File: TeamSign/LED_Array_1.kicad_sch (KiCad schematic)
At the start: 56 parts

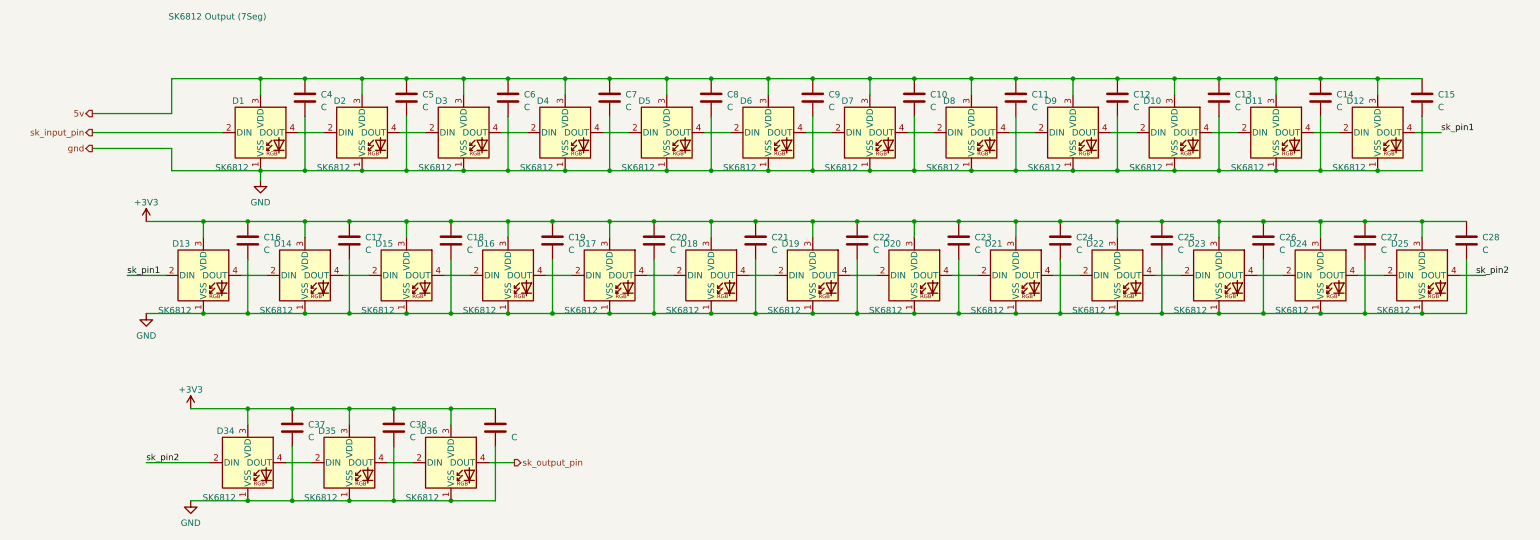
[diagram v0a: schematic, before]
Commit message: Add PEM nut footprint starter to library, also did small tweaks to BOM and updated symbols to include the barrel jack antics.  Yay!
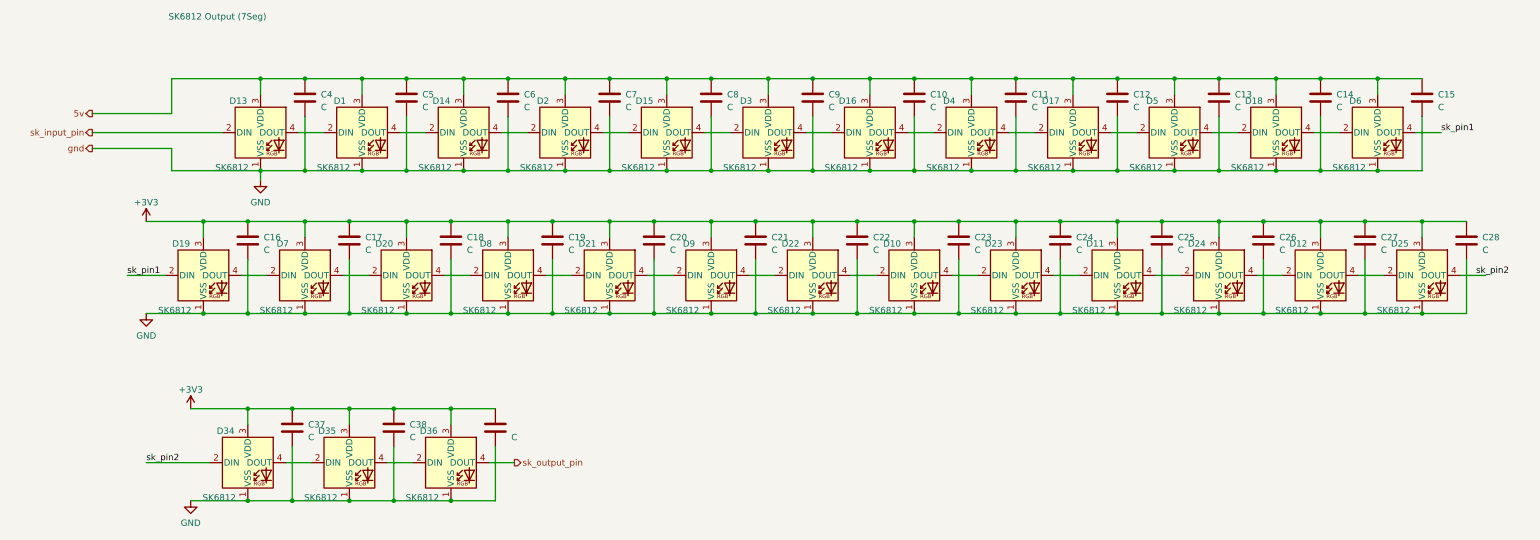
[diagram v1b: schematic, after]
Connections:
- net +3V3: now also D10.3 (VDD), D11.3 (VDD), D12.3 (VDD), D7.3 (VDD), D8.3 (VDD), D9.3 (VDD); no longer D13.3 (VDD), D14.3 (VDD), D15.3 (VDD), D16.3 (VDD), D17.3 (VDD), D18.3 (VDD)
- net 5v: now also D13.3 (VDD), D14.3 (VDD), D15.3 (VDD), D16.3 (VDD), D17.3 (VDD), D18.3 (VDD); no longer D10.3 (VDD), D11.3 (VDD), D12.3 (VDD), D7.3 (VDD), D8.3 (VDD), D9.3 (VDD)
- net sk_input_pin: now also D13.2 (DIN); no longer D1.2 (DIN)
- net sk_pin1: now also D19.2 (DIN), D6.4 (DOUT); no longer D12.4 (DOUT), D13.2 (DIN)
- net at D17.2 (DIN): now also D4.4 (DOUT); no longer D16.4 (DOUT)
- net at D17.4 (DOUT): now also D5.2 (DIN); no longer D18.2 (DIN)
- net at D2.2 (DIN): now also D14.4 (DOUT); no longer D1.4 (DOUT)
- net at D2.4 (DOUT): now also D15.2 (DIN); no longer D3.2 (DIN)
- net at D6.2 (DIN): now also D18.4 (DOUT); no longer D5.4 (DOUT)
- net at D7.2 (DIN): now also D19.4 (DOUT); no longer D6.4 (DOUT)
- net at D8.2 (DIN): now also D20.4 (DOUT); no longer D7.4 (DOUT)
- net at D8.4 (DOUT): now also D21.2 (DIN); no longer D9.2 (DIN)
- net at D9.4 (DOUT): now also D22.2 (DIN); no longer D10.2 (DIN)
- net at D15.4 (DOUT): now also D3.2 (DIN); no longer D16.2 (DIN)
- net at D20.2 (DIN): now also D7.4 (DOUT); no longer D19.4 (DOUT)
- net at D21.4 (DOUT): now also D9.2 (DIN); no longer D22.2 (DIN)
- net at D22.4 (DOUT): now also D10.2 (DIN); no longer D23.2 (DIN)
- net at D23.4 (DOUT): now also D11.2 (DIN); no longer D24.2 (DIN)
- net at D4.2 (DIN): now also D16.4 (DOUT); no longer D3.4 (DOUT)
- net at D10.4 (DOUT): now also D23.2 (DIN); no longer D11.2 (DIN)
- net at D11.4 (DOUT): now also D24.2 (DIN); no longer D12.2 (DIN)
- net at D24.4 (DOUT): now also D12.2 (DIN); no longer D25.2 (DIN)
- net at D13.4 (DOUT): now also D1.2 (DIN); no longer D14.2 (DIN)
- new net: D18.2 (DIN), D5.4 (DOUT)
- new net: D16.2 (DIN), D3.4 (DOUT)
- new net: D12.4 (DOUT), D25.2 (DIN)
- new net: D1.4 (DOUT), D14.2 (DIN)
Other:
- moved on the sheet: D1, D10, D11, D12, D13, D14, D15, D16, D17, D18, D19, D2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

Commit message: Place caps :)
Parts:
- removed C10, C11, C12, C13, C14, C15, C16, C17, C18, C19, C20, C21, C22, C23, C24, C25, C26, C27, C28, C37, C38, C39, C5, C6, C7, C8, C9: C, symbol Device:C
- added C4 (x27): 100nF, Capacitor_SMD:C_1206_3216Metric_Pad1.33x1.80mm_HandSolder, symbol Device:C
- C4: value C -> 100nF; footprint (none) -> Capacitor_SMD:C_1206_3216Metric_Pad1.33x1.80mm_HandSolder
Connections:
- net +3V3: now also C4.1, C4.1, C4.1, C4.1, C4.1, C4.1, C4.1, C4.1, C4.1, C4.1, C4.1, C4.1, C4.1, C4.1, C4.1, C4.1
- net 5v: now also C4.1, C4.1, C4.1, C4.1, C4.1, C4.1, C4.1, C4.1, C4.1, C4.1, C4.1
- net GND: now also C4.2, C4.2, C4.2, C4.2, C4.2, C4.2, C4.2, C4.2, C4.2, C4.2, C4.2, C4.2, C4.2, C4.2, C4.2, C4.2, C4.2, C4.2, C4.2, C4.2, C4.2, C4.2, C4.2, C4.2, C4.2, C4.2, C4.2

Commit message: Resolve subsheet antics... Yay.
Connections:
- net +3V3 is gone; now on net 5v: C4.1, C4.1, C4.1, C4.1, C4.1, C4.1, C4.1, C4.1, C4.1, C4.1, C4.1, C4.1, C4.1, C4.1, C4.1, C4.1, D10.3 (VDD), D11.3 (VDD), D12.3 (VDD), D19.3 (VDD), D20.3 (VDD), D21.3 (VDD), D22.3 (VDD), D23.3 (VDD), D24.3 (VDD), D25.3 (VDD), D34.3 (VDD), D35.3 (VDD), D36.3 (VDD), D7.3 (VDD), D8.3 (VDD), D9.3 (VDD)
- net sk_input_pin: now also D19.2 (DIN); no longer D13.2 (DIN)
- net sk_output_pin: now also D25.4 (DOUT); no longer D36.4 (DOUT)
- net sk_pin1: now also D15.2 (DIN), D21.4 (DOUT); no longer D19.2 (DIN), D6.4 (DOUT)
- net sk_pin2: now also D12.2 (DIN), D18.4 (DOUT); no longer D25.4 (DOUT), D34.2 (DIN)
- net at D17.2 (DIN): now also D23.4 (DOUT); no longer D4.4 (DOUT)
- net at D17.4 (DOUT): now also D11.2 (DIN); no longer D5.2 (DIN)
- net at D34.4 (DOUT): now also D13.2 (DIN); no longer D35.2 (DIN)
- net at D2.2 (DIN): now also D8.4 (DOUT); no longer D14.4 (DOUT)
- net at D2.4 (DOUT): now also D21.2 (DIN); no longer D15.2 (DIN)
- net at D6.2 (DIN): now also D12.4 (DOUT); no longer D18.4 (DOUT)
- net at D8.2 (DIN): now also D14.4 (DOUT); no longer D20.4 (DOUT)
- net at D9.2 (DIN): now also D15.4 (DOUT); no longer D21.4 (DOUT)
- net at D9.4 (DOUT): now also D3.2 (DIN); no longer D22.2 (DIN)
- net at D19.4 (DOUT): now also D34.2 (DIN); no longer D7.2 (DIN)
- net at D7.4 (DOUT): now also D35.2 (DIN); no longer D20.2 (DIN)
- net at D18.2 (DIN): now also D24.4 (DOUT); no longer D5.4 (DOUT)
- net at D22.4 (DOUT): now also D16.2 (DIN); no longer D10.2 (DIN)
- net at D23.2 (DIN): now also D4.4 (DOUT); no longer D10.4 (DOUT)
- net at D4.2 (DIN): now also D10.4 (DOUT); no longer D16.4 (DOUT)
- net at D36.2 (DIN): now also D20.4 (DOUT); no longer D35.4 (DOUT)
- net at D11.4 (DOUT): now also D5.2 (DIN); no longer D24.2 (DIN)
- net at D3.4 (DOUT): now also D22.2 (DIN); no longer D16.2 (DIN)
- net at D25.2 (DIN): now also D6.4 (DOUT); no longer D12.4 (DOUT)
- net at D13.4 (DOUT): now also D7.2 (DIN); no longer D1.2 (DIN)
- net at D1.4 (DOUT): now also D20.2 (DIN); no longer D14.2 (DIN)
- new net: D24.2 (DIN), D5.4 (DOUT)
- new net: D1.2 (DIN), D35.4 (DOUT)
- new net: D10.2 (DIN), D16.4 (DOUT)
- new net: D14.2 (DIN), D36.4 (DOUT)
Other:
- moved on the sheet: D1, D10, D12, D13, D14, D15, D16, D17, D18, D19, D2, D20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
